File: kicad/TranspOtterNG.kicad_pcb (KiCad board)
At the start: 2 copper layers, 65.3 x 38.1 mm, 31 parts, among them J1 UART/I2C, J2 UART/IO/ANALOG, J3 Display, J4 GameTrak, J6 Nunchuk, J7 VCC, U1 AMS1117

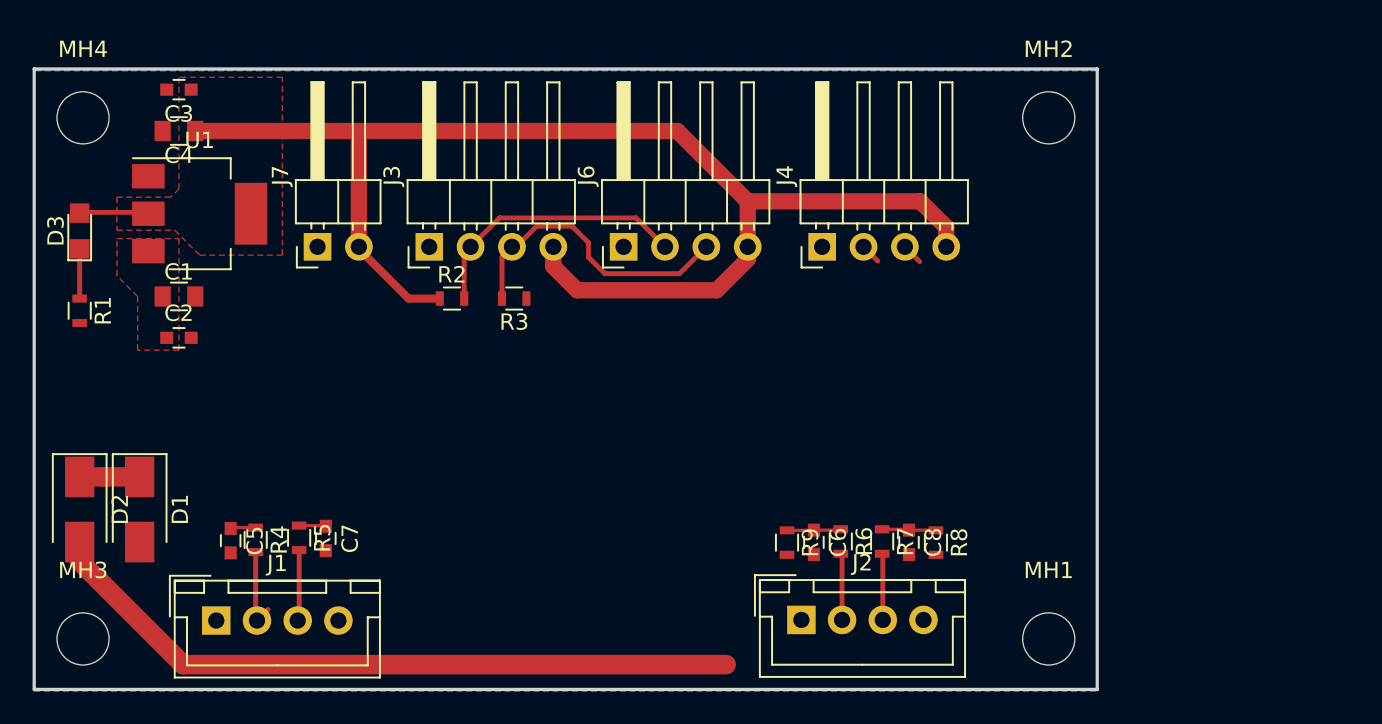
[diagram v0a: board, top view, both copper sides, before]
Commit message: added stepdown
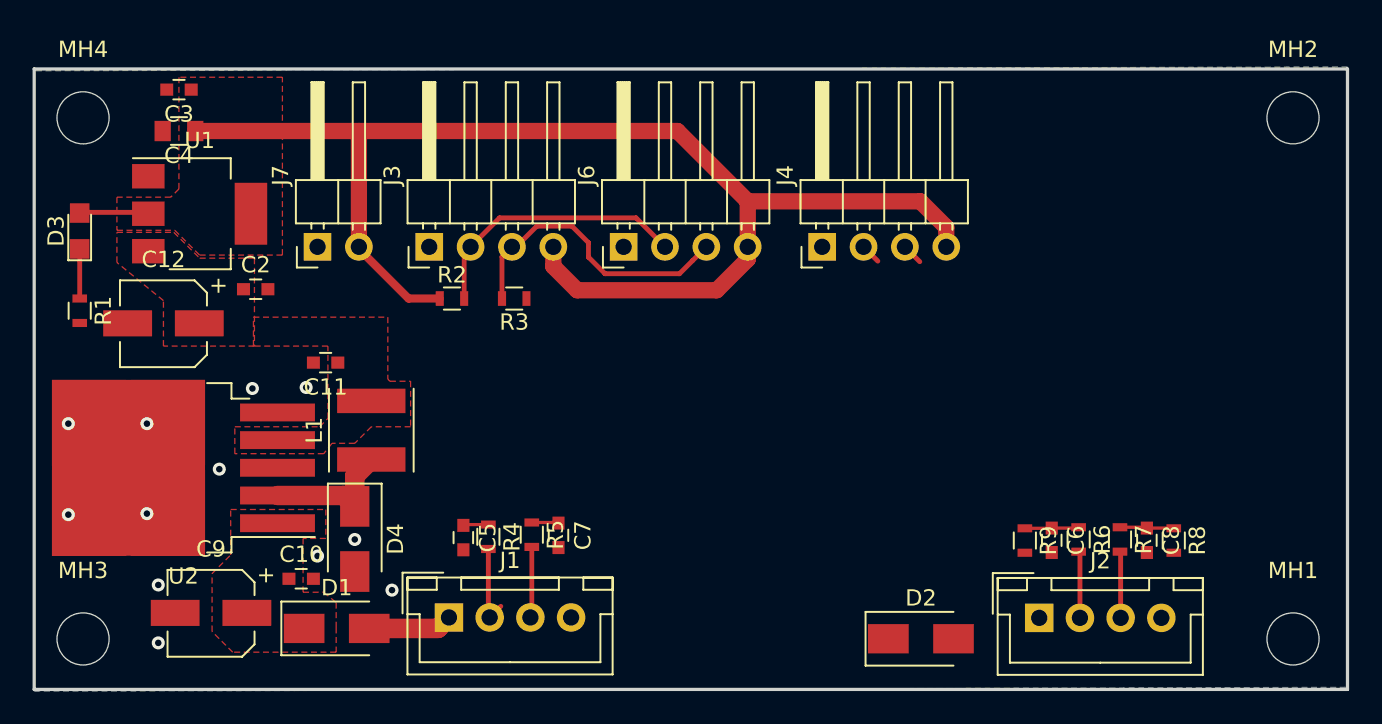
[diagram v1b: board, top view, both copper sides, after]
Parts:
- removed C1: 1u, Capacitors_SMD:C_0805
- added C10: 100n, Capacitors_SMD:C_0603, F.Cu at (123.1, 82.1)
- added C11: 100n, Capacitors_SMD:C_0603, F.Cu at (124.6, 68.8)
- added C12: 470u, Capacitors_SMD:CP_Elec_5x5.3, F.Cu at (114.6, 66.4)
- added C9: 470u, Capacitors_SMD:CP_Elec_5x5.3, F.Cu at (117.5, 84.2)
- added D4: 1N5822, Diodes_SMD:D_SMA, F.Cu at (126.4, 79.7)
- added L1: L, Inductors_SMD:L_Taiyo-Yuden_MD-5050, F.Cu at (127.4, 73.0)
- added U2: LM2596S-5, TO_SOT_Packages_SMD:TO-263-5_TabPin3, F.Cu at (115.8, 75.3)
- moved D2 52.3 mm to (161.1, 85.8), turned to 0 degrees
- moved MH1 15.0 mm to (184.0, 85.8)
- moved MH2 15.0 mm to (184.0, 53.8)
- moved J2 14.6 mm to (168.4, 84.5)
- moved R8 14.6 mm to (176.7, 79.8)
- moved R9 14.6 mm to (167.5, 79.8)
- moved C6 14.6 mm to (169.2, 79.7)
- moved C8 14.6 mm to (175.0, 79.7)
- moved R6 14.6 mm to (170.8, 79.7)
- moved R7 14.6 mm to (173.4, 79.7)
- moved C7 14.3 mm to (138.9, 79.4)
- moved J1 14.3 mm to (132.1, 84.5)
- moved C5 14.3 mm to (133.0, 79.6)
- moved R4 14.3 mm to (134.6, 79.5)
- moved R5 14.3 mm to (137.2, 79.4)
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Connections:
- C2 pad 1: +15V -> +5V
- U1 pad 3: +15V -> +5V
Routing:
- net Net-(D2-Pad2): track 43.5 -> 0.00 mm
- net Net-(D4-Pad1): track 0.00 -> 8.32 mm
- net Net-(D1-Pad2): track 0.00 -> 5.17 mm
- net +15V: track 3.68 -> 0.00 mm
- net GND: vias 0 -> 12
- added copper zone on F.Cu, net +5V
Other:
- board size 65.3 x 38.1 mm -> 80.6 x 38.1 mm

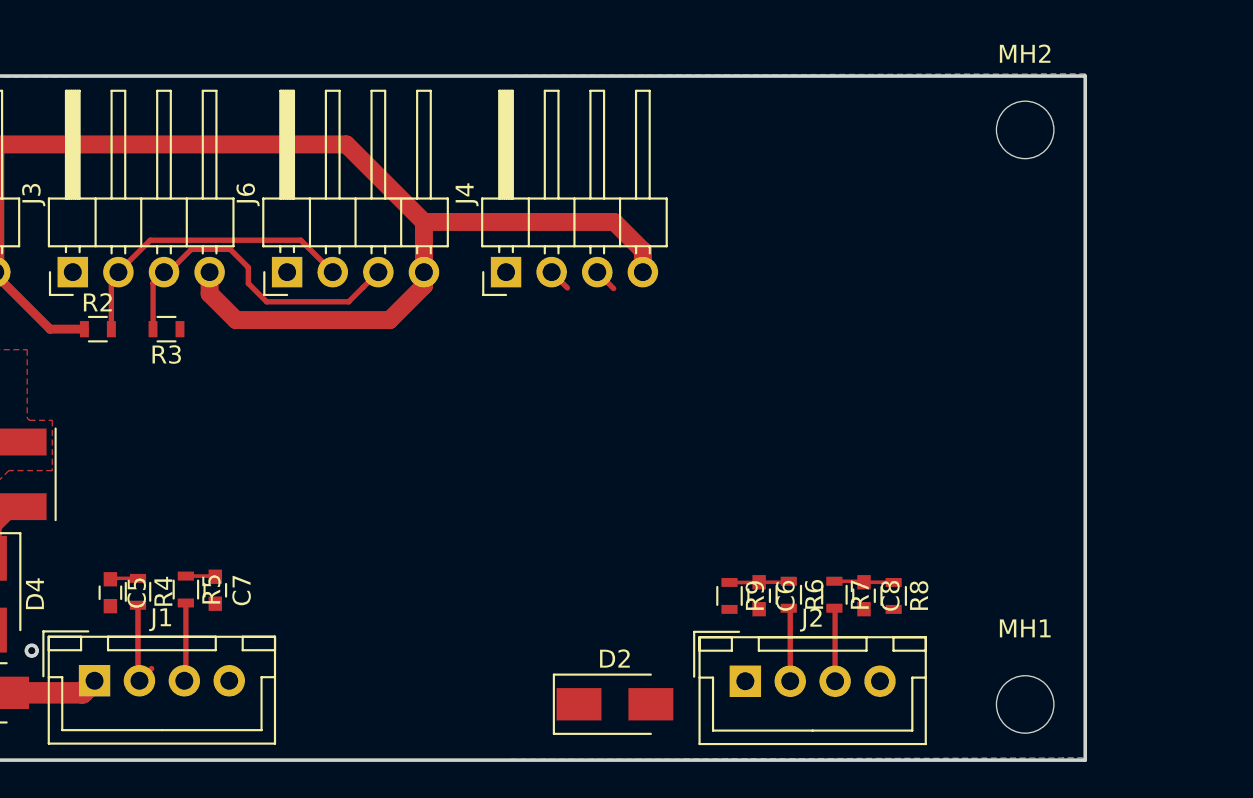
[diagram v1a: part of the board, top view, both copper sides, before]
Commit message: added esp and rfm
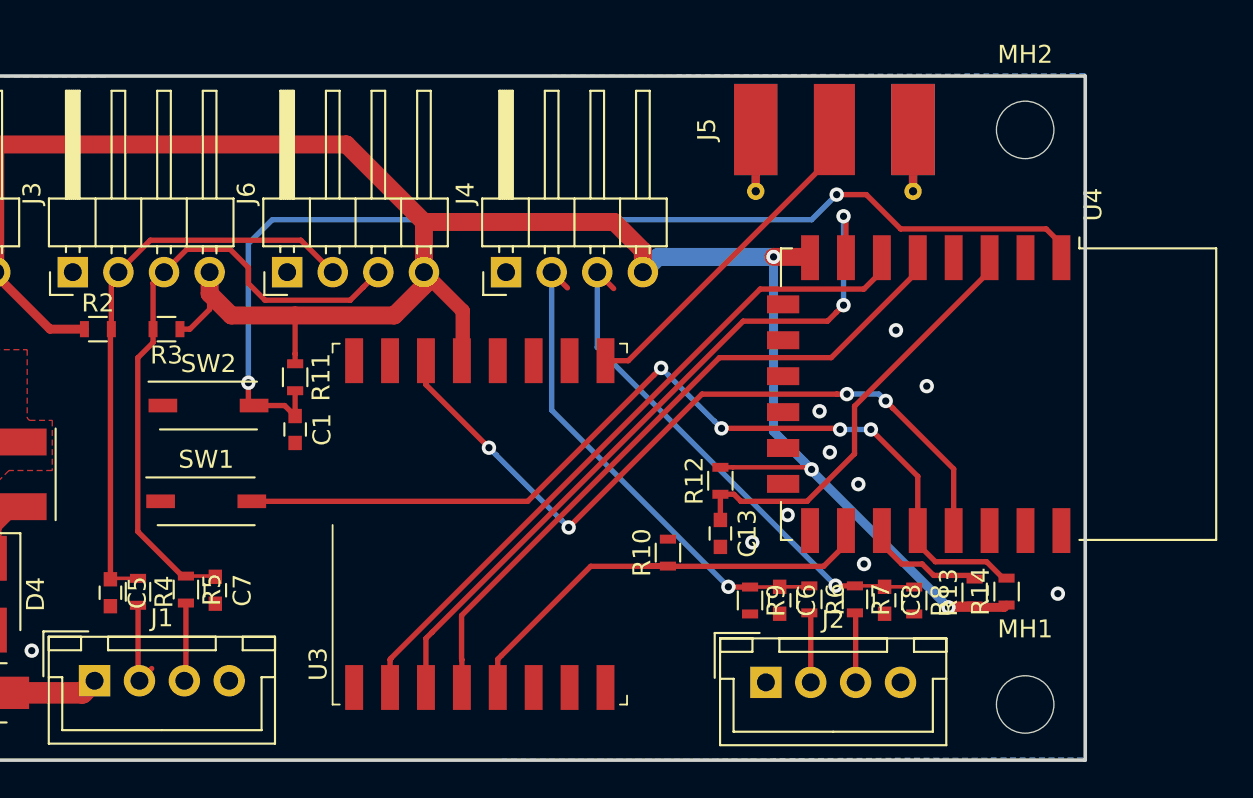
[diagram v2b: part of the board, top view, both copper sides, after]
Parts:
- removed D2: 1N4001, Diodes_SMD:D_SMA
- added C1: 100n, Capacitors_SMD:C_0603, F.Cu at (143.3, 70.5)
- added C13: 100n, Capacitors_SMD:C_0603, F.Cu at (167.0, 76.3)
- added J5: Ant, Connectors_Molex:Molex_SMA_Jack_Edge_Mount, F.Cu at (173.4, 55.5)
- added R10: 10k, Resistors_SMD:R_0603, F.Cu at (164.1, 77.3)
- added R11: 10k, Resistors_SMD:R_0603, F.Cu at (143.3, 67.6)
- added R12: 10k, Resistors_SMD:R_0603, F.Cu at (167.0, 73.3)
- added R13: 10k, Resistors_SMD:R_0603, F.Cu at (181.2, 79.6)
- added R14: 10k, Resistors_SMD:R_0603, F.Cu at (182.9, 79.5)
- added SW1: Flash, Buttons_Switches_SMD:SW_DIP_x1_W5.08mm_Slide_Copal_CHS-A, F.Cu at (138.4, 74.5)
- added SW2: Reset, Buttons_Switches_SMD:SW_DIP_x1_W5.08mm_Slide_Copal_CHS-A, F.Cu at (138.5, 69.2)
- added U3: RFM69HCW, RF_Modules:HOPERF-RFM69HW, F.Cu at (153.6, 75.8)
- added U4: ESP-12E, RF_Modules:ESP-12E, F.Cu at (182.5, 68.5)
- moved C6 1.17 mm to (170.3, 80.0)
- moved C8 1.17 mm to (176.1, 80.0)
- moved R6 1.17 mm to (172.0, 79.9)
- moved R7 1.17 mm to (174.5, 79.9)
- moved R8 1.17 mm to (177.8, 80.0)
- moved R9 1.17 mm to (168.7, 80.0)
- moved J2 1.14 mm to (169.5, 84.6)
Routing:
- net RESET: track 0.00 -> 61.0 mm, vias 0 -> 2
- net VCC: track 85.8 -> 139.3 mm, vias 0 -> 3
- net GPIO0: track 0.00 -> 52.2 mm, vias 0 -> 4
- net GPIO4: track 0.00 -> 42.4 mm, vias 0 -> 4
- net MOSI: track 0.00 -> 41.0 mm, vias 0 -> 2
- net MISO: track 0.00 -> 38.7 mm
- net SCK: track 0.00 -> 38.1 mm
- net NSS: track 0.00 -> 25.3 mm
- net Net-(C13-Pad1): track 0.00 -> 24.2 mm
- net RX1_ADC2: track 4.62 -> 28.7 mm, vias 0 -> 1
- net TX1_ADC1: track 4.57 -> 27.4 mm, vias 0 -> 1
- net ANT: track 0.00 -> 18.9 mm
- net RX0_SDA: track 20.3 -> 35.6 mm
- net TX0_SCL: track 18.5 -> 32.5 mm
- net Net-(R13-Pad2): track 0.00 -> 6.72 mm
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
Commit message: added programming header
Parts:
- added J8: Conn_01x05_Male, Pin_Headers:Pin_Header_Straight_1x05_Pitch2.54mm, F.Cu at (164.3, 85.3)
- moved R10 13.2 mm to (155.4, 87.4), turned to 0 degrees
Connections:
- R13 pad 1: VCC -> Net-(R13-Pad1)
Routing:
- net GPIO5: track 0.00 -> 30.3 mm
- net TXD_ESP: track 0.00 -> 28.6 mm
- net RXD_ESP: track 0.00 -> 28.3 mm
- net VCC: track 139.3 -> 143.1 mm
- net NSS: track 25.3 -> 26.9 mm
- net GND: vias 21 -> 22

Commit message: moved libraries
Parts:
- removed J5: Ant, Connectors_Molex:Molex_SMA_Jack_Edge_Mount
- added AE1: Antenna_Loop, otter:868MHZ Inverted-F, F.Cu at (137.3, 35.8)
- added C14: C_Small, Capacitor_SMD:C_0603_1608Metric, F.Cu at (182.0, 44.0)
- C1, C10, C11, C13, C2, C3, C5, C6, C7, C8: footprint Capacitors_SMD:C_0603 -> Capacitor_SMD:C_0603_1608Metric
- C12, C9: footprint Capacitors_SMD:CP_Elec_5x5.3 -> Capacitor_SMD:CP_Elec_5x5.3
- C4: footprint Capacitors_SMD:C_0805 -> Capacitor_SMD:C_0805_2012Metric
- D1, D4: footprint Diodes_SMD:D_SMA -> Diode_SMD:D_SMA
- D3: footprint LEDs:LED_0805 -> LED_SMD:LED_0805_2012Metric
- J1, J2: footprint Connectors_JST:JST_XH_B04B-XH-A_04x2.50mm_Straight -> Connector_JST:JST_XH_B04B-XH-A_1x04_P2.50mm_Vertical
- J3, J4, J6: footprint Pin_Headers:Pin_Header_Angled_1x04_Pitch2.54mm -> Connector_PinHeader_2.54mm:PinHeader_1x04_P2.54mm_Horizontal
- J7: footprint Pin_Headers:Pin_Header_Angled_1x02_Pitch2.54mm -> Connector_PinHeader_2.54mm:PinHeader_1x02_P2.54mm_Horizontal
- J8: footprint Pin_Headers:Pin_Header_Straight_1x05_Pitch2.54mm -> Connector_PinHeader_2.54mm:PinHeader_1x05_P2.54mm_Vertical
- L1: footprint Inductors_SMD:L_Taiyo-Yuden_MD-5050 -> Inductor_SMD:L_Taiyo-Yuden_MD-5050
- MH1, MH2, MH3, MH4: footprint Mounting_Holes:MountingHole_3.2mm_M3 -> MountingHole:MountingHole_3.2mm_M3
- R1, R10, R11, R12, R13, R14, R2, R3, R4, R5, R6, R7, R8, R9: footprint Resistors_SMD:R_0603 -> Resistor_SMD:R_0603_1608Metric
- SW1, SW2: footprint Buttons_Switches_SMD:SW_DIP_x1_W5.08mm_Slide_Copal_CHS-A -> Button_Switch_SMD:SW_DIP_SPSTx01_Slide_Copal_CHS-01A_W5.08mm_P1.27mm_JPin
- U1: footprint TO_SOT_Packages_SMD:SOT-223-3_TabPin2 -> Package_TO_SOT_SMD:SOT-223-3_TabPin2
- U2: footprint TO_SOT_Packages_SMD:TO-263-5_TabPin3 -> Package_TO_SOT_SMD:TO-263-5_TabPin3
- U3: footprint RF_Modules:HOPERF-RFM69HW -> RF_Module:HOPERF_RFM69HW
- U4: footprint RF_Modules:ESP-12E -> RF_Module:ESP-12E
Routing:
- net ANT: track 18.9 -> 0.00 mm

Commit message: v1 finished
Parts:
- removed AE1: Antenna_Loop, otter:868MHZ Inverted-F
- removed J7: VCC, Connector_PinHeader_2.54mm:PinHeader_1x02_P2.54mm_Horizontal
- added Antenna: Antenna, Connector_Pin:Pin_D1.0mm_L10.0mm, F.Cu at (187.1, 79.5)
- added G***: LOGO, otter:otter_small25, F.Cu at (143.2, 72.5)
- added POWER: Power, Connector_PinHeader_2.54mm:PinHeader_1x03_P2.54mm_Horizontal, F.Cu at (123.7, 61.7)
- moved C14 40.1 mm to (184.1, 84.0), turned to 225 degrees
- moved J8 38.5 mm to (194.1, 61.0), turned to 0 degrees
- moved R10 31.8 mm to (183.9, 73.0)
- moved C1 26.5 mm to (165.8, 56.5)
- moved R11 26.5 mm to (165.8, 53.6)
- moved C6 23.0 mm to (147.3, 80.0)
- moved C8 23.0 mm to (153.1, 80.0)
- moved J2 23.0 mm to (146.5, 84.6)
- moved R6 23.0 mm to (149.0, 79.9)
- moved R7 23.0 mm to (151.5, 79.9)
- moved R8 23.0 mm to (154.8, 80.0)
- moved R9 23.0 mm to (145.7, 80.0)
- moved C13 21.6 mm to (168.3, 54.7), turned to 90 degrees
- moved R14 20.2 mm to (189.6, 60.5)
- moved R13 17.7 mm to (189.6, 64.0), turned to 270 degrees
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- renumbered SW1 to BOOT, J3 to DISPLAY, U4 to ESP8266, J4 to GAMETRAK, J6 to NUNCHUK, SW2 to RESET, U3 to RFM69
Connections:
- R13 pad 1: Net-(R13-Pad1) -> VCC
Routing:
- net RESET: track 61.0 -> 28.6 mm
- net VCC: track 143.1 -> 173.3 mm
- net MOSI: track 41.0 -> 19.0 mm, vias 2 -> 0
- net MISO: track 38.7 -> 19.0 mm
- net GPIO4: track 42.4 -> 22.9 mm, vias 4 -> 0
- net Net-(C13-Pad1): track 24.2 -> 4.77 mm
- net TXD_ESP: track 28.6 -> 12.1 mm
- net GPIO5: track 30.3 -> 14.1 mm
- net RXD_ESP: track 28.3 -> 13.2 mm
- net SCK: track 38.1 -> 26.6 mm
- net NSS: track 26.9 -> 37.2 mm
- net +5V: track 0.00 -> 7.90 mm
- net GPIO0: track 52.2 -> 44.4 mm, vias 4 -> 0
- net ANT: track 0.00 -> 5.94 mm
- net Net-(AE1-Pad1): track 0.00 -> 4.96 mm
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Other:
- board size 80.6 x 38.1 mm -> 90.6 x 38.1 mm
- board text added: "+5V"
- board text added: "1"
- board text added: "A1"
- board text added: "A2"
- board text added: "GND"
- board text added: "RX"
- board text added: "SCL"
- board text added: "SDA"
- board text added: "TX"
- board text added: "TranspOtterNG"
- board text added: "VCC"

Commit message: minor changes, now v2
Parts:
- removed Antenna: Antenna, Connector_Pin:Pin_D1.0mm_L10.0mm
- removed BOOT: Flash, Button_Switch_SMD:SW_DIP_SPSTx01_Slide_Copal_CHS-01A_W5.08mm_P1.27mm_JPin
- removed C11: 100n, Capacitor_SMD:C_0603_1608Metric
- removed D4: 1N5822, Diode_SMD:D_SMA
- removed DISPLAY: Display, Connector_PinHeader_2.54mm:PinHeader_1x04_P2.54mm_Horizontal
- removed ESP8266: ESP-12E, RF_Module:ESP-12E
- removed GAMETRAK: GameTrak, Connector_PinHeader_2.54mm:PinHeader_1x04_P2.54mm_Horizontal
- removed L1: L, Inductor_SMD:L_Taiyo-Yuden_MD-5050
- removed NUNCHUK: Nunchuk, Connector_PinHeader_2.54mm:PinHeader_1x04_P2.54mm_Horizontal
- removed POWER: Power, Connector_PinHeader_2.54mm:PinHeader_1x03_P2.54mm_Horizontal
- removed RESET: Reset, Button_Switch_SMD:SW_DIP_SPSTx01_Slide_Copal_CHS-01A_W5.08mm_P1.27mm_JPin
- removed RFM69: RFM69HCW, RF_Module:HOPERF_RFM69HW
- added AE1: Antenna, Connector_Pin:Pin_D1.0mm_L10.0mm, F.Cu at (190.4, 80.8)
- added J3: Conn_01x04_Male, Connector_PinHeader_2.54mm:PinHeader_1x04_P2.54mm_Vertical, F.Cu at (114.6, 65.6)
- added J4: GameTrak, Connector_PinHeader_2.54mm:PinHeader_1x04_P2.54mm_Vertical, F.Cu at (103.4, 73.6)
- added J7: xt30, otter:XT60_angle, F.Cu at (194.4, 70.2)
- added J9: Conn_01x16_Female, Connector_PinHeader_2.54mm:PinHeader_1x16_P2.54mm_Vertical, F.Cu at (120.6, 42.5)
- added P1: CONN_WII, otter:CONN_WII, F.Cu at (108.5, 47.0)
- added Q1: Q_NMOS_GDS, Package_TO_SOT_SMD:SOT-23, F.Cu at (107.8, 72.4)
- added Q2: Q_PMOS_GDS, Package_TO_SOT_SMD:TO-252-2, F.Cu at (133.2, 80.5)
- added R15: 100k, Resistor_SMD:R_0603_1608Metric, F.Cu at (108.0, 76.7)
- added R16: 100k, Resistor_SMD:R_0603_1608Metric, F.Cu at (108.0, 75.0)
- added R17: 100k, Resistor_SMD:R_0603_1608Metric, F.Cu at (111.3, 71.3)
- added R18: 10k, Resistor_SMD:R_0603_1608Metric, F.Cu at (130.0, 45.6)
- added R19: 10k, Resistor_SMD:R_0603_1608Metric, F.Cu at (129.9, 47.1)
- added R20: 10k, Resistor_SMD:R_0603_1608Metric, F.Cu at (129.9, 48.6)
- added R21: DNP, Resistor_SMD:R_0603_1608Metric, F.Cu at (133.9, 45.6)
- added R22: DNP, Resistor_SMD:R_0603_1608Metric, F.Cu at (134.0, 47.1)
- added R23: DNP, Resistor_SMD:R_0603_1608Metric, F.Cu at (133.9, 48.6)
- added R26: 220, Resistor_SMD:R_0603_1608Metric, F.Cu at (160.6, 55.4)
- added R27: 10k, Resistor_SMD:R_0603_1608Metric, F.Cu at (127.7, 48.7)
- added R28: 10k, Resistor_SMD:R_0603_1608Metric, F.Cu at (127.7, 45.6)
- added SW1: Flash, Button_Switch_SMD:SW_DIP_SPSTx01_Slide_Copal_CHS-01A_W5.08mm_P1.27mm_JPin, F.Cu at (193.3, 51.4)
- added SW2: Reset, Button_Switch_SMD:SW_DIP_SPSTx01_Slide_Copal_CHS-01A_W5.08mm_P1.27mm_JPin, F.Cu at (197.6, 51.4)
- added U3: RFM69HCW, RF_Module:HOPERF_RFM69HW, F.Cu at (171.4, 74.9)
- added U4: ESP-12E, RF_Module:ESP-12E, F.Cu at (174.3, 52.0)
- added U5: PCF8574, Package_SO:SOIC-16W_7.5x10.3mm_P1.27mm, F.Cu at (151.0, 50.1)
- C12, C9: value 470u -> 20u
- D1: value 1N4001 -> 12V; footprint Diode_SMD:D_SMA -> Diode_SMD:D_SMB
- U2: value LM2596S-5 -> URB4805YMD-6WR3; footprint Package_TO_SOT_SMD:TO-263-5_TabPin3 -> otter:URB4805YMD-6WR3
- moved C10 50.0 mm to (158.2, 46.5), turned to 270 degrees
- moved D3 49.6 mm to (158.6, 67.8)
- moved R1 49.6 mm to (158.6, 72.7)
- moved C3 44.2 mm to (158.9, 60.5), turned to 90 degrees
- moved C4 41.9 mm to (157.0, 60.4), turned to 90 degrees
- moved C12 34.8 mm to (149.1, 70.5)
- moved C2 34.8 mm to (154.8, 68.4)
- moved U1 34.8 mm to (151.4, 63.8)
- moved R3 22.8 mm to (120.8, 49.0), turned to 90 degrees
- moved J1 22.6 mm to (109.9, 80.7)
- moved C5 22.6 mm to (110.8, 76.0)
- moved C7 22.6 mm to (116.5, 76.0)
- moved R4 22.6 mm to (112.3, 76.0)
- moved R5 22.6 mm to (115.0, 76.0)
- moved R2 21.8 mm to (119.1, 49.0), turned to 90 degrees
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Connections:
- C10 pad 1: +15V -> +5V
- C9 pad 1: +15V -> Net-(C9-Pad1)
- D1 pad 1: +15V -> Net-(D1-Pad1)
- J1 pad 1: Net-(D1-Pad2) -> +15V
- R13 pad 2: Net-(R13-Pad2) -> WS2812
- U2 pad 1: +15V -> GND
- U2 pad 2: Net-(D4-Pad1) -> Net-(C9-Pad1)
- U2 pad 3: GND -> +5V
- U2 pad 4: +5V -> (no net)
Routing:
- net +5V: track 7.90 -> 111.3 mm
- net WS2812: track 0.00 -> 74.3 mm, vias 0 -> 3
- net Net-(D1-Pad1): track 0.00 -> 67.0 mm, vias 0 -> 1
- net RX0_SDA: track 35.1 -> 91.3 mm, vias 0 -> 3
- net TX0_SCL: track 33.7 -> 79.6 mm, vias 0 -> 3
- net Net-(D1-Pad2): track 5.17 -> 38.7 mm
- net RX1_ADC2: track 25.9 -> 57.3 mm
- net GPIO0: track 44.4 -> 16.5 mm
- net TX1_ADC1: track 24.3 -> 51.1 mm
- net VCC: track 173.3 -> 148.4 mm, vias 3 -> 5
- net RS: track 0.00 -> 21.0 mm, vias 0 -> 1
- net RW: track 0.00 -> 20.8 mm
- net Net-(C9-Pad1): track 0.00 -> 19.0 mm
- net CS: track 0.00 -> 17.1 mm
- net A2: track 0.00 -> 16.7 mm, vias 0 -> 2
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- removed copper zone on F.Cu, net +15V
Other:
- board size 90.6 x 38.1 mm -> 100 x 45 mm
- board text added: "Boot"
- board text added: "Display"
- board text added: "ESP8266"
- board text added: "Gametrak"
- board text added: "INT"
- board text added: "Nunchuk"
- board text added: "Power In"
- board text added: "RFM69"
- board text added: "Reset"
- board text added: "WS2812"
- board text removed: "1"
- board text removed: "SCL"
- board text removed: "SDA"
